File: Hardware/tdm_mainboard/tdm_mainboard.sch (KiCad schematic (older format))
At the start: 72 parts, among them IC1 W25Q128JVSIQ, J1 Headphone, J2 LineIn, J3 Conn_02x06_Top_Bottom, U1 AP7313, U2 PAM8302AASCR, U3 SGTL5000, U4 Teensy4, U5 TPS61090RSAR, U6 MOUNTINGHOLE2.5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

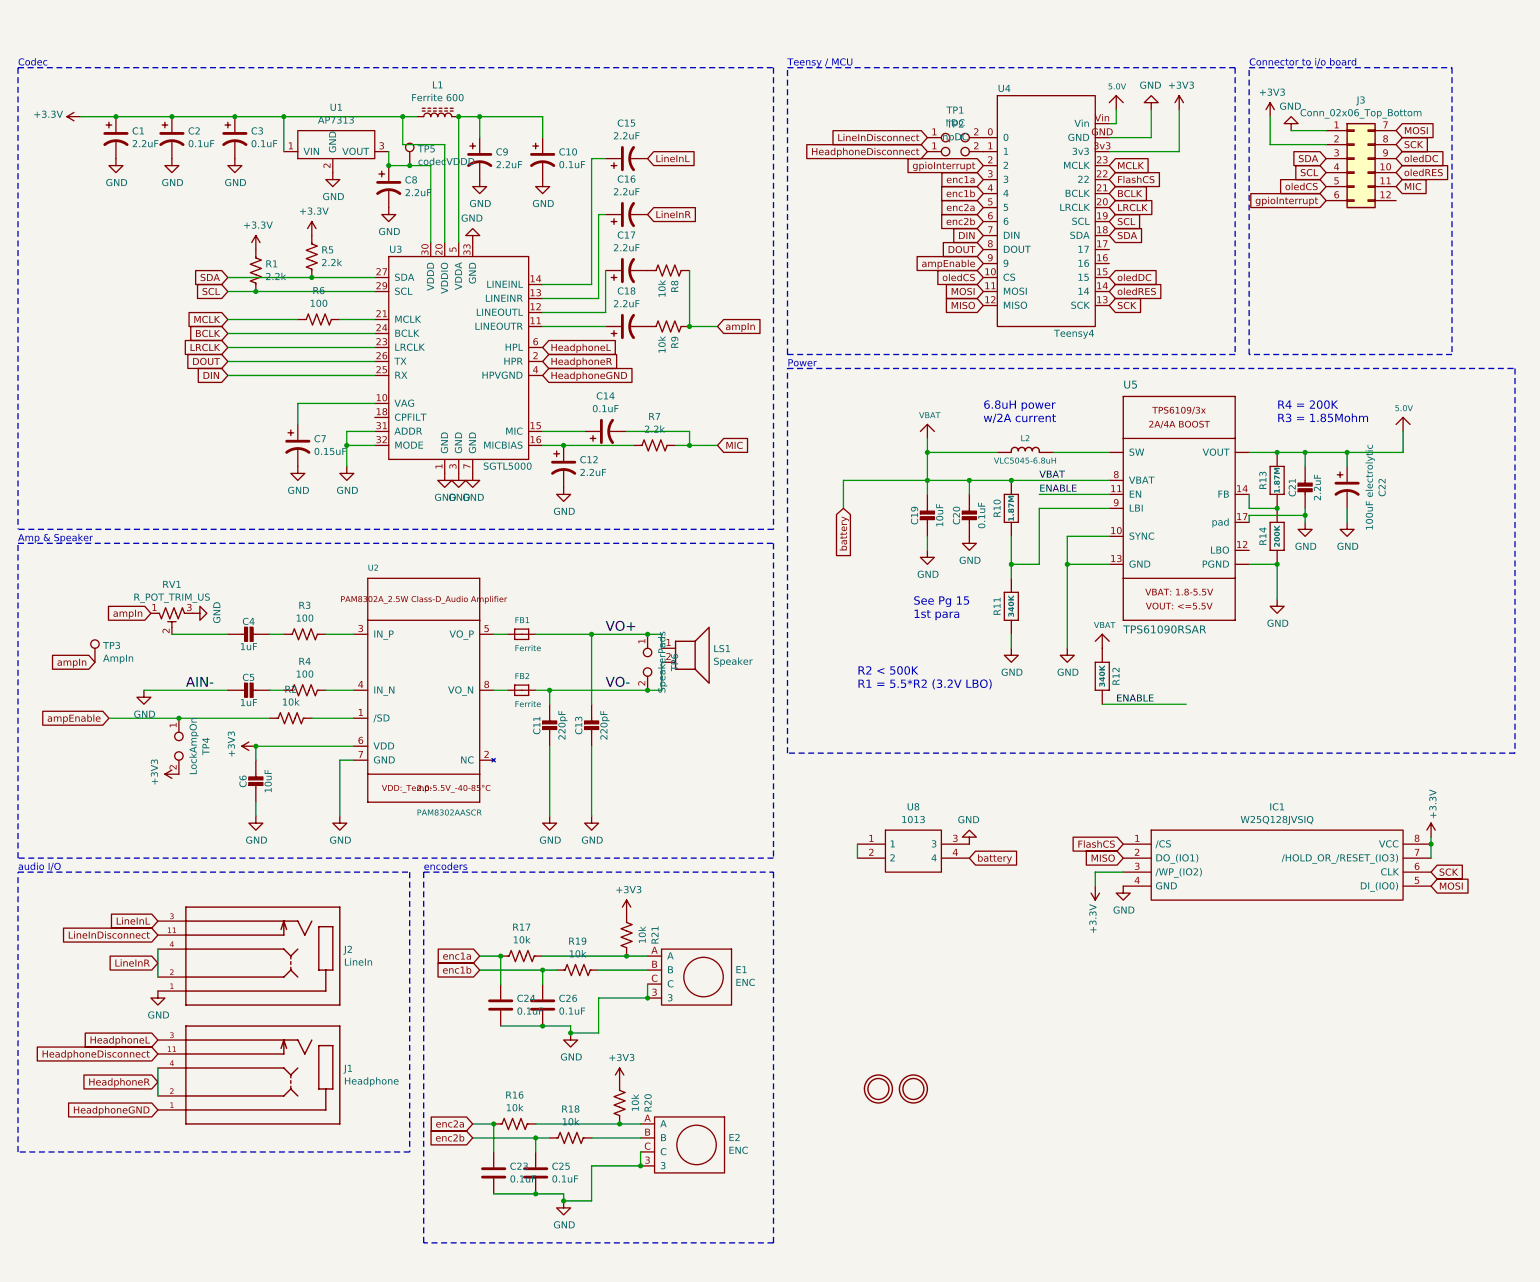
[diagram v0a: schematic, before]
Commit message: playing around with samd11 for the frontboard, reworked power on the back
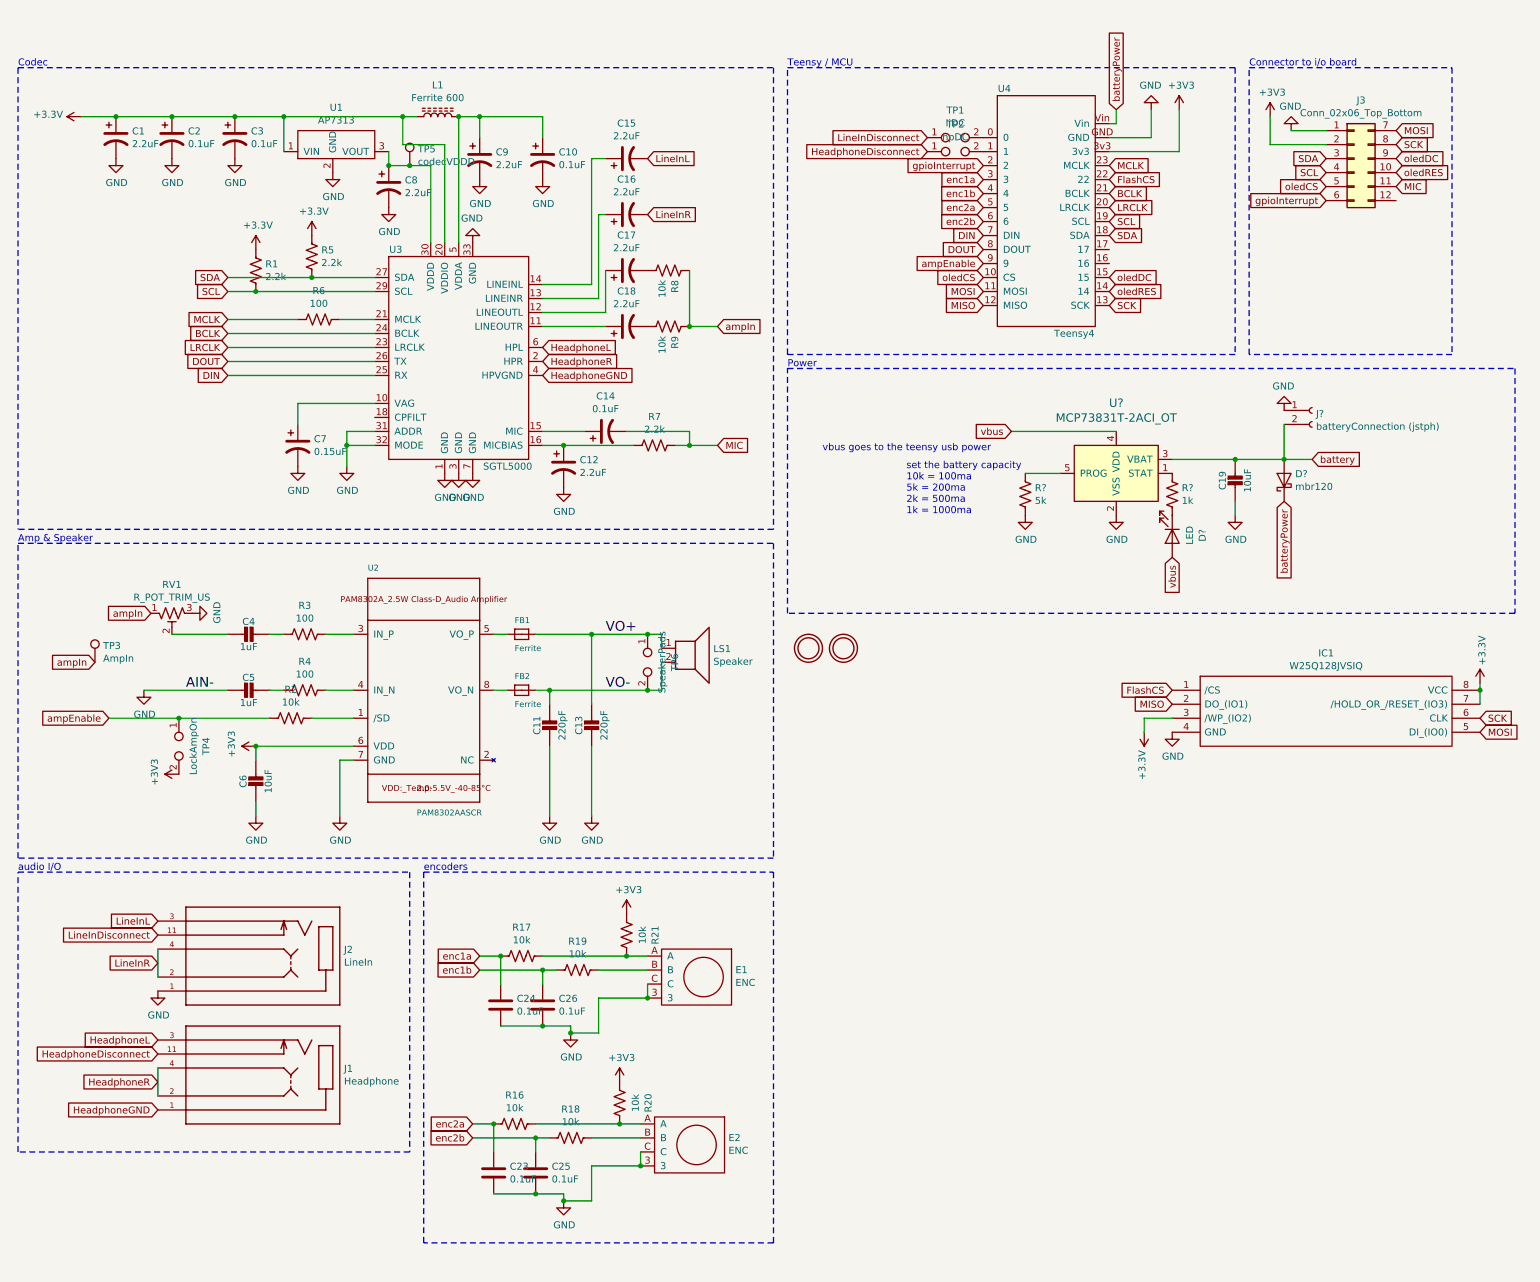
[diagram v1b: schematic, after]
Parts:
- removed C20: 0.1uF, Capacitors_SMD:C_0603, symbol tdm_mainboard-eagle-import:CAP_CERAMIC0805-NOOUTLINE
- removed C21: 2.2uF, Capacitors_SMD:C_0603, symbol tdm_mainboard-eagle-import:CAP_CERAMIC0805-NOOUTLINE
- removed C22: 100uF electrolytic, Capacitors_Tantalum_SMD:CP_Tantalum_Case-A_EIA-3216-18_Reflow, symbol Device:CP1
- removed L2: VLC5045-6.8uH, SamacSys_Parts:INDPM5050X450N, symbol tdm_mainboard-eagle-import:INDUCTORTDK_VLC5045
- removed R10, R13: 1.87M, Resistors_SMD:R_0603, symbol tdm_mainboard-eagle-import:RESISTOR0805_NOOUTLINE
- removed R11, R12: 340K, Resistors_SMD:R_0603, symbol tdm_mainboard-eagle-import:RESISTOR0805_NOOUTLINE
- removed R14: 200K, Resistors_SMD:R_0603, symbol tdm_mainboard-eagle-import:RESISTOR0805_NOOUTLINE
- removed U5: TPS61090RSAR, SamacSys_Parts:QFN65P400X400X100-17N, symbol tdm_mainboard-eagle-import:VREG_TPS6103X
- removed U8: 1013, SamacSys_Parts:1013, symbol SamacSys_Parts:1013
- added D?: LED, symbol Device:LED
- added D?: mbr120, symbol Device:D_Schottky
- added J?: batteryConnection (jstph), symbol Connector:Conn_01x02_Female
- added R?: 1k, Resistors_SMD:R_0603, symbol Device:R_US
- added R?: 5k, symbol Device:R_US
- added U?: MCP73831T-2ACI_OT, digikey-footprints:SOT-753, symbol dk_PMIC-Battery-Chargers:MCP73831T-2ACI_OT
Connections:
- net GND: now also J?.1 (Pin_1), R?.2, U?.2 (VSS)
- net battery: now also D?.2 (A), J?.2 (Pin_2), U?.3 (VBAT)
- net batteryPower: now reaches U4.Vin
- net batteryPower: now also D?.1 (K)
- new net: R?.1, U?.1 (STAT)
- new net: R?.1, U?.5 (PROG)
- new net: D?.1 (K), R?.2
- new net vbus: D?.2 (A), U?.4 (VDD)
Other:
- note added: "set the battery capacity\n10k = 100ma\n5k = 200ma\n2k = 500ma\n1k = 1000ma"
- note added: "vbus goes to the teensy usb power"
- note removed: "6.8uH power\nw/2A current"
- note removed: "R2 < 500K\nR1 = 5.5*R2 (3.2V LBO)"
- note removed: "R4 = 200K\nR3 = 1.85Mohm"
- note removed: "See Pg 15\n1st para"
- moved on the sheet: C19, IC1

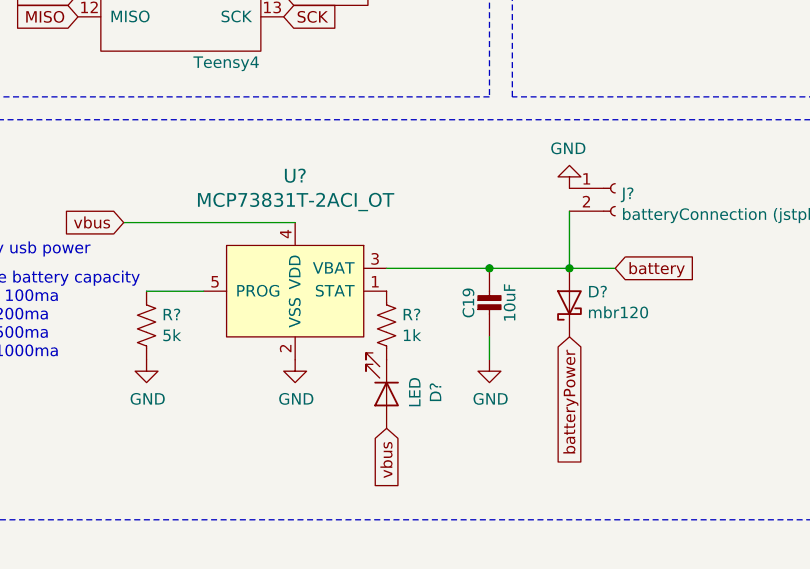
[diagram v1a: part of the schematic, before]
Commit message: added annotations to mainboard
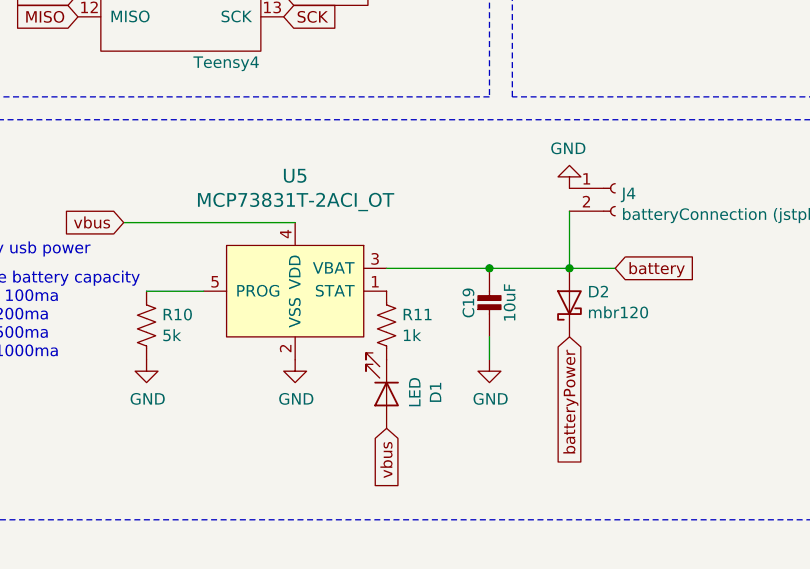
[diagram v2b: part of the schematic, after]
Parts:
- gave numbers to parts that had none: 6
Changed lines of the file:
@@
 ampEnable
 $Comp
-L dk_PMIC-Battery-Chargers:MCP73831T-2ACI_OT U?
+L dk_PMIC-Battery-Chargers:MCP73831T-2ACI_OT U5
 U 1 1 5E885055
 P 8550 3500
-F 0 "U?" H 8550 3903 60  0000 C CNN
+F 0 "U5" H 8550 3903 60  0000 C CNN
 F 1 "MCP73831T-2ACI_OT" H 8550 3797 60  0000 C CNN
 F 2 "digikey-footprints:SOT-753" H 8750 3700 60  0001 L CNN
@@
 $EndComp
 $Comp
-L Device:R_US R?
+L Device:R_US R11
 U 1 1 5E8CD984
 P 8950 3750
-F 0 "R?" H 9018 3796 50  0000 L CNN
+F 0 "R11" H 9018 3796 50  0000 L CNN
 F 1 "1k" H 9018 3705 50  0000 L CNN
 F 2 "Resistors_SMD:R_0603" V 8990 3740 50  0001 C CNN
@@
 $EndComp
 $Comp
-L Device:LED D?
+L Device:LED D1
 U 1 1 5E8DF0D6
 P 8950 4050
-F 0 "D?" H 8943 4266 50  0000 C CNN
+F 0 "D1" H 8943 4266 50  0000 C CNN
 F 1 "LED" H 8943 4175 50  0000 C CNN
 F 2 "" H 8950 4050 50  0001 C CNN
@@
 	9400 3500 8950 3500
 $Comp
-L power:GND #PWR?
+L power:GND #PWR0123
 U 1 1 5E92A1A7
 P 8550 3900
-F 0 "#PWR?" H 8550 3650 50  0001 C CNN
+F 0 "#PWR0123" H 8550 3650 50  0001 C CNN
 F 1 "GND" H 8555 3727 50  0000 C CNN
 F 2 "" H 8550 3900 50  0001 C CNN
@@
 set the battery capacity\n10k = 100ma\n5k = 200ma\n2k = 500ma\n1k = 1000ma
 $Comp
-L Device:R_US R?
+L Device:R_US R10
 U 1 1 5E955C15
 P 7900 3750
-F 0 "R?" H 7968 3796 50  0000 L CNN
+F 0 "R10" H 7968 3796 50  0000 L CNN
 F 1 "5k" H 7968 3705 50  0000 L CNN
 F 2 "" V 7940 3740 50  0001 C CNN
@@
 	8150 3600 7900 3600
 $Comp
-L power:GND #PWR?
+L power:GND #PWR0124
 U 1 1 5E961452
 P 7900 3900
-F 0 "#PWR?" H 7900 3650 50  0001 C CNN
+F 0 "#PWR0124" H 7900 3650 50  0001 C CNN
 F 1 "GND" H 7905 3727 50  0000 C CNN
 F 2 "" H 7900 3900 50  0001 C CNN
@@
 $EndComp
 $Comp
-L Device:D_Schottky D?
+L Device:D_Schottky D2
 U 1 1 5E980CCB
 P 9750 3650
-F 0 "D?" V 9796 3571 50  0000 R CNN
+F 0 "D2" V 9796 3571 50  0000 R CNN
 F 1 "mbr120" V 9705 3571 50  0000 R CNN
 F 2 "" H 9750 3650 50  0001 C CNN
@@
 batteryPower
 $Comp
-L Connector:Conn_01x02_Female J?
+L Connector:Conn_01x02_Female J4
 U 1 1 5E9C1334
 P 9950 3150
-F 0 "J?" H 9978 3126 50  0000 L CNN
+F 0 "J4" H 9978 3126 50  0000 L CNN
 F 1 "batteryConnection (jstph)" H 9978 3035 50  0000 L CNN
 F 2 "" H 9950 3150 50  0001 C CNN
@@
 	9750 3250 9750 3500
 $Comp
-L power:GND #PWR?
+L power:GND #PWR0125
 U 1 1 5E9E4400
 P 9750 3150
-F 0 "#PWR?" H 9750 2900 50  0001 C CNN
+F 0 "#PWR0125" H 9750 2900 50  0001 C CNN
 F 1 "GND" H 9755 2977 50  0000 C CNN
 F 2 "" H 9750 3150 50  0001 C CNN
